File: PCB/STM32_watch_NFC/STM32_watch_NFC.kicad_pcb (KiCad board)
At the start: 4 copper layers, 37 x 37 mm, 159 parts, among them J1 Conn_01x06_Socket, J2 USB_C_Receptacle_PowerOnly_6P, Q1 2N7000, SW1 SW_DPST_x2, SW2 SW_DPST_x2, SW3 SW_DPST_x2, U1 STM32L031G6Ux, U2 MIC5365-3.3YC5, U4 MT3608, Y2 32.768kHz

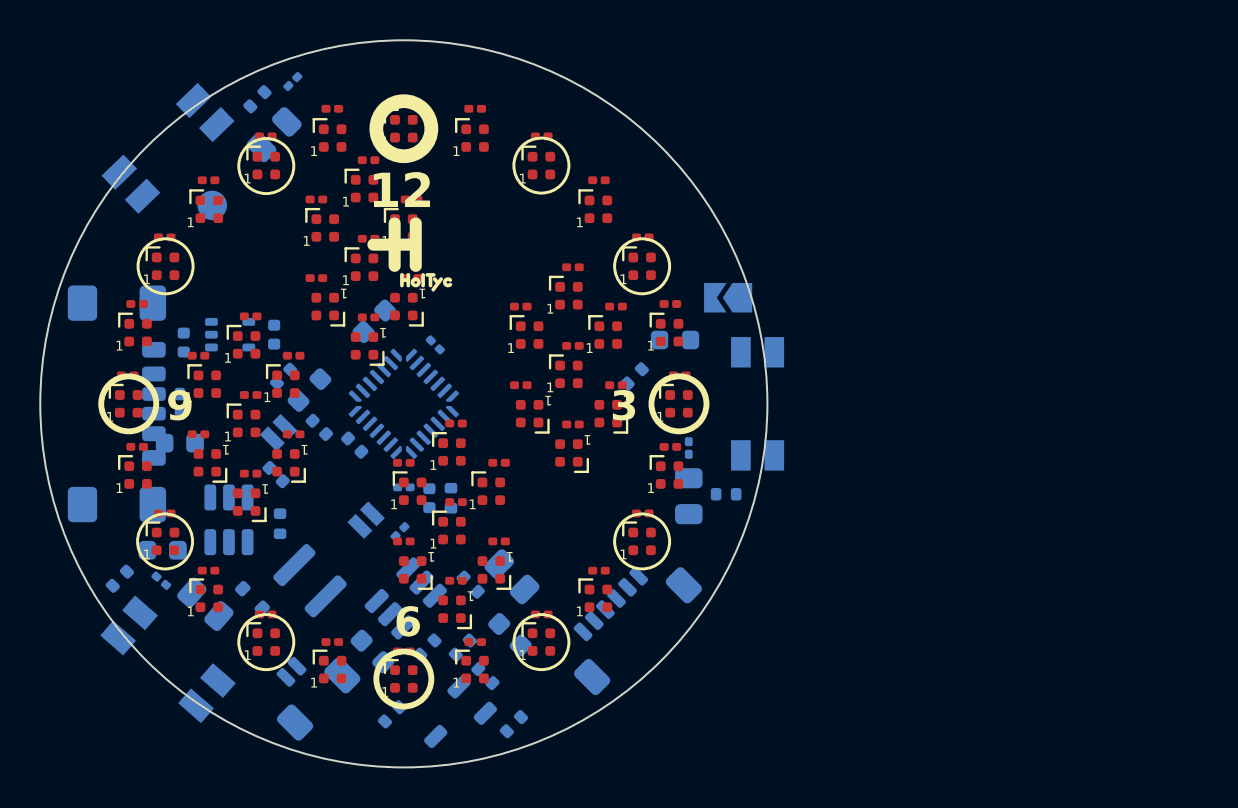
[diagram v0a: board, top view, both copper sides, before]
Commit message: Kicad - new Routing 3
TM1637 7-segment driver
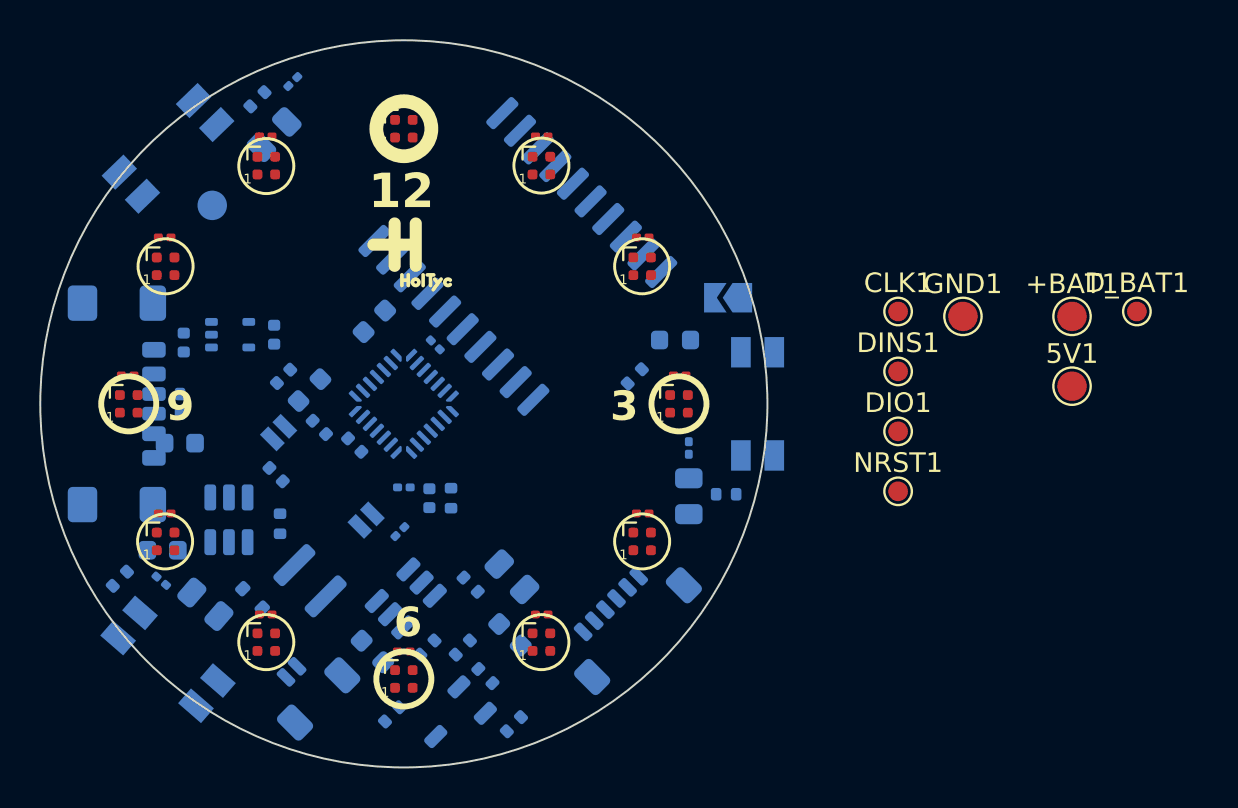
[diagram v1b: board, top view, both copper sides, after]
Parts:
- removed the C13 at (152.1, 117.1)
- removed the C15 at (158.4, 113.5)
- removed the C17 at (162.1, 107.2)
- removed the C19 at (162.1, 99.9)
- removed the C21 at (158.4, 93.6)
- removed the C23 at (152.1, 90.0)
- removed C32, C34, C36, C38, C40, C42, C43, C44, C45, C46, C47, C48, C49, C50, C51, C52, C53, C54, C55, C56, C57, C58, C59, C60, C61, C62, C63, C64, C65, C66, C67, C68, C69, C70: 100n, Capacitor_SMD:C_0201_0603Metric
- removed the D10 at (158.4, 95.1)
- removed the D12 at (152.1, 91.5)
- removed D16, D18, D20, D22, D24, D26, D27, D28, D29, D30, D31, D32, D33, D34, D35, D36, D37, D38, D39, D40, D43, D44, D45, D46, D47, D48, D49, D50, D51, D52, D53, D54: SK6805, LED_SMD:LED_SK6812_EC15_1.5x1.5mm
- removed the D2 at (152.1, 118.5)
- removed the D4 at (158.4, 114.9)
- removed the D41 at (140.5, 110.0)
- removed the D42 at (142.5, 108.0)
- removed the D6 at (162.0, 108.6)
- removed the D8 at (162.0, 101.4)
- added +BAT1: 2.7-4.2V, TestPoint:TestPoint_Pad_D1.5mm, F.Cu at (182.5, 100.5)
- added 5V1: 5V, TestPoint:TestPoint_Pad_D1.5mm, F.Cu at (182.5, 104.1)
- added CLK1: ~, TestPoint:TestPoint_Pad_D1.0mm, F.Cu at (173.7, 100.3)
- added DINS1: ~, TestPoint:TestPoint_Pad_D1.0mm, F.Cu at (173.7, 103.3)
- added DIO1: ~, TestPoint:TestPoint_Pad_D1.0mm, F.Cu at (173.7, 106.4)
- added D_BAT1: ~, TestPoint:TestPoint_Pad_D1.0mm, F.Cu at (185.8, 100.3)
- added GND1: GND, TestPoint:TestPoint_Pad_D1.5mm, F.Cu at (176.9, 100.5)
- added NRST1: ~, TestPoint:TestPoint_Pad_D1.0mm, F.Cu at (173.7, 109.5)
- added U3: TM1637, Package_SO:SOP-20_7.5x12.8mm_P1.27mm, B.Cu at (154.3, 97.5)
- renumbered C31 to C12, C22 to C13, C20 to C14, C18 to C15, C14 to C17, C12 to C18, C41 to C19, C39 to C20, C37 to C21, C35 to C22, C33 to C23, D15 to D1, D21 to D10, D19 to D11, D17 to D12, D11 to D2, D9 to D3, D7 to D4, D13 to D41, D14 to D42, D3 to D6, D1 to D7, D25 to D8, D23 to D9
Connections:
- D1 pad 1: Net-(D15-DOUT) -> Net-(D1-DOUT)
- D1 pad 3: Net-(D12-DOUT) -> Net-(D1-DIN)
- D10 pad 1: Net-(D21-DOUT) -> Net-(D10-DOUT)
- D10 pad 3: Net-(D20-DOUT) -> Net-(D10-DIN)
- D11 pad 1: Net-(D19-DOUT) -> Net-(D11-DOUT)
- D11 pad 3: Net-(D18-DOUT) -> Net-(D10-DOUT)
- D12 pad 1: Net-(D17-DOUT) -> unconnected-(D12-DOUT-Pad1)
- D12 pad 3: Net-(D16-DOUT) -> Net-(D11-DOUT)
- D2 pad 1: Net-(D11-DOUT) -> Net-(D2-DOUT)
- D2 pad 3: Net-(D10-DOUT) -> Net-(D1-DOUT)
- D3 pad 1: Net-(D10-DIN) -> Net-(D3-DOUT)
- D3 pad 3: Net-(D8-DOUT) -> Net-(D2-DOUT)
- D4 pad 1: Net-(D7-DOUT) -> Net-(D4-DOUT)
- D4 pad 3: Net-(D6-DOUT) -> Net-(D3-DOUT)
- D6 pad 1: Net-(D3-DOUT) -> Net-(D6-DOUT)
- D6 pad 3: Net-(D2-DOUT) -> Net-(D5-DOUT)
- D7 pad 1: Net-(D1-DOUT) -> Net-(D7-DOUT)
- D7 pad 3: Net-(D1-DIN) -> Net-(D6-DOUT)
- D8 pad 1: Net-(D25-DOUT) -> Net-(D8-DOUT)
- D8 pad 3: Net-(D25-DIN) -> Net-(D7-DOUT)
- D9 pad 1: Net-(D23-DOUT) -> Net-(D10-DIN)
- D9 pad 3: Net-(D22-DOUT) -> Net-(D8-DOUT)

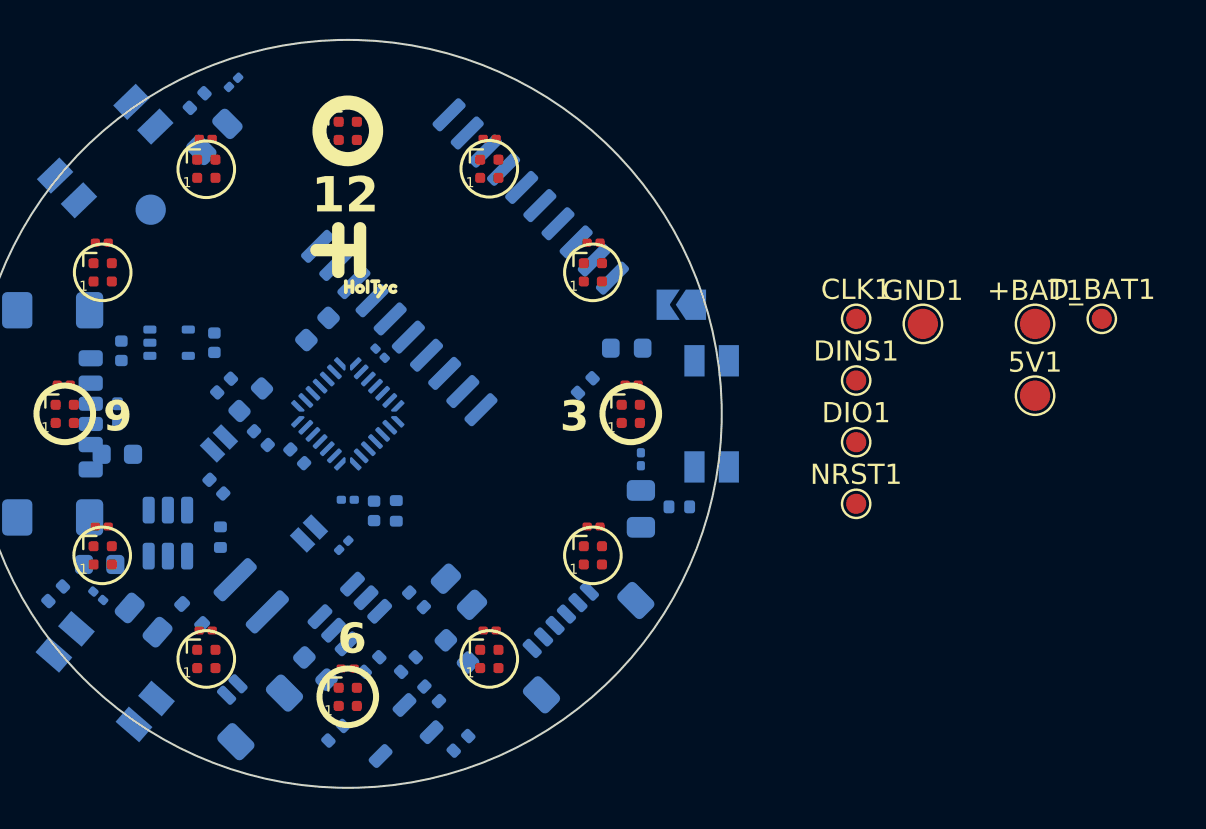
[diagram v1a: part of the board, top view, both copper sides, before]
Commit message: Kicad - new Routing 4.5
NEW 7-segment display + connection, new charger, charging status
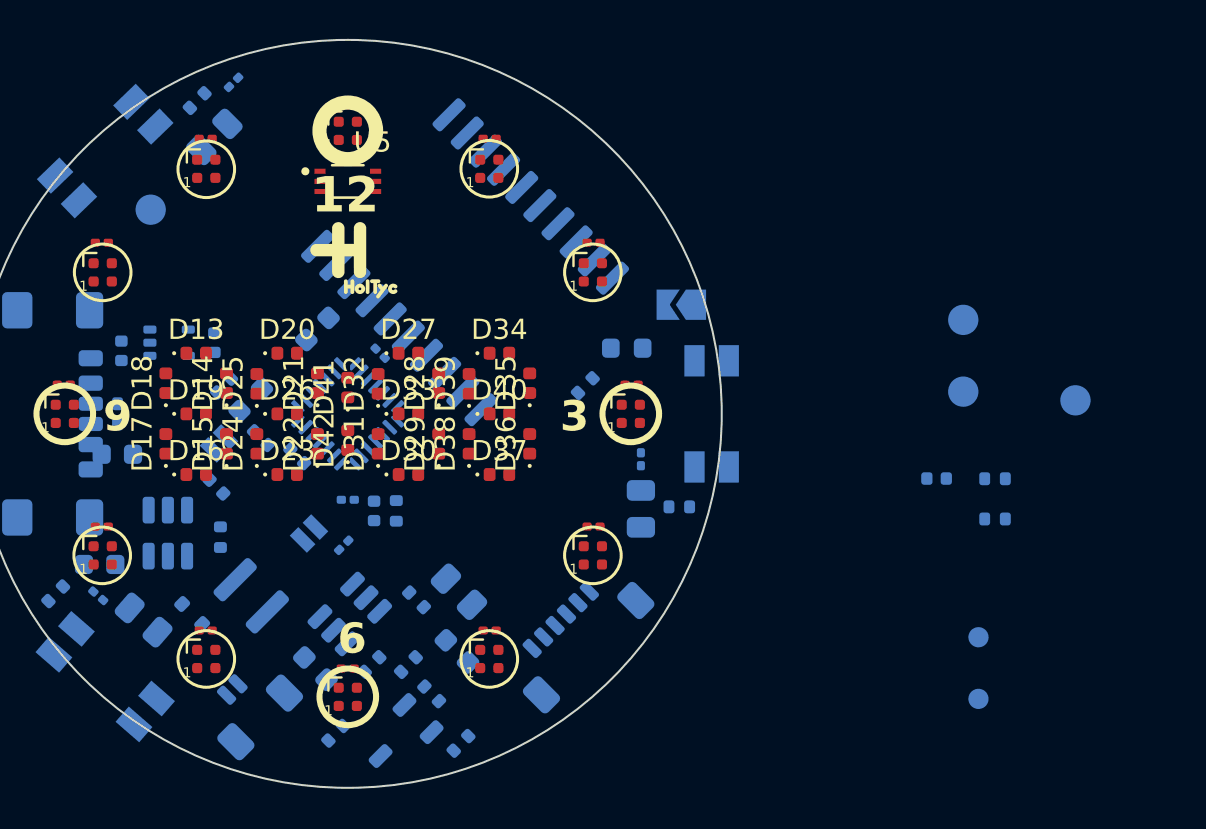
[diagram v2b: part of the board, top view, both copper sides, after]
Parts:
- removed CLK1, DINS1, DIO1, D_BAT1, NRST1: ~, TestPoint:TestPoint_Pad_D1.0mm
- added C31: 1u, Capacitor_SMD:C_0402_1005Metric, B.Cu at (177.6, 108.2)
- added D13: LED, LED_SMD:LED_0402_1005Metric, F.Cu at (141.0, 102.0)
- added D14: LED, LED_SMD:LED_0402_1005Metric, F.Cu at (142.5, 103.5)
- added D15: LED, LED_SMD:LED_0402_1005Metric, F.Cu at (142.5, 106.5)
- added D16: LED, LED_SMD:LED_0402_1005Metric, F.Cu at (141.0, 108.0)
- added D17: LED, LED_SMD:LED_0402_1005Metric, F.Cu at (139.5, 106.5)
- added D18: LED, LED_SMD:LED_0402_1005Metric, F.Cu at (139.5, 103.5)
- added D19: LED, LED_SMD:LED_0402_1005Metric, F.Cu at (141.0, 105.0)
- added D20: LED, LED_SMD:LED_0402_1005Metric, F.Cu at (145.5, 102.0)
- added D21: LED, LED_SMD:LED_0402_1005Metric, F.Cu at (147.0, 103.5)
- added D22: LED, LED_SMD:LED_0402_1005Metric, F.Cu at (147.0, 106.5)
- added D23: LED, LED_SMD:LED_0402_1005Metric, F.Cu at (145.5, 108.0)
- added D24: LED, LED_SMD:LED_0402_1005Metric, F.Cu at (144.0, 106.5)
- added D25: LED, LED_SMD:LED_0402_1005Metric, F.Cu at (144.0, 103.5)
- added D26: LED, LED_SMD:LED_0402_1005Metric, F.Cu at (145.5, 105.0)
- added D27: LED, LED_SMD:LED_0402_1005Metric, F.Cu at (151.5, 102.0)
- added D28: LED, LED_SMD:LED_0402_1005Metric, F.Cu at (153.0, 103.5)
- added D29: LED, LED_SMD:LED_0402_1005Metric, F.Cu at (153.0, 106.5)
- added D30: LED, LED_SMD:LED_0402_1005Metric, F.Cu at (151.5, 108.0)
- added D31: LED, LED_SMD:LED_0402_1005Metric, F.Cu at (150.0, 106.5)
- added D32: LED, LED_SMD:LED_0402_1005Metric, F.Cu at (150.0, 103.5)
- added D33: LED, LED_SMD:LED_0402_1005Metric, F.Cu at (151.5, 105.0)
- added D34: LED, LED_SMD:LED_0402_1005Metric, F.Cu at (156.0, 102.0)
- added D35: LED, LED_SMD:LED_0402_1005Metric, F.Cu at (157.5, 103.5)
- added D36: LED, LED_SMD:LED_0402_1005Metric, F.Cu at (157.5, 106.5)
- added D37: LED, LED_SMD:LED_0402_1005Metric, F.Cu at (156.0, 108.0)
- added D38: LED, LED_SMD:LED_0402_1005Metric, F.Cu at (154.5, 106.5)
- added D39: LED, LED_SMD:LED_0402_1005Metric, F.Cu at (154.5, 103.5)
- added D40: LED, LED_SMD:LED_0402_1005Metric, F.Cu at (156.0, 105.0)
- added D41: LED, LED_SMD:LED_0402_1005Metric, F.Cu at (148.5, 103.7)
- added D42: LED, LED_SMD:LED_0402_1005Metric, F.Cu at (148.5, 106.3)
- added DINLED1: ~, TestPoint:TestPoint_Pad_D1.0mm, B.Cu at (179.7, 116.0)
- added DINSTM2: ~, TestPoint:TestPoint_Pad_D1.0mm, B.Cu at (179.7, 119.1)
- added R20: 510, Resistor_SMD:R_0402_1005Metric, B.Cu at (180.5, 108.2)
- added R21: 510, Resistor_SMD:R_0402_1005Metric, B.Cu at (180.5, 110.2)
- added U5: BH1750FVI-TR, BH1750FVI-TR:XDCR_BH1750FVI-TR, F.Cu at (148.5, 93.5)
- +BAT1, 5V1, GND1: moved to B.Cu
- moved GND1 8.44 mm to (184.5, 104.3), turned to 180 degrees
- moved +BAT1 3.56 mm to (178.9, 100.3), turned to 180 degrees
- moved 5V1 3.56 mm to (178.9, 103.9), turned to 180 degrees
- renumbered D41 to D43, D42 to D44
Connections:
- U1 pad 25: unconnected-(U1-PB6-Pad25) -> SCL_LIGHT
- U1 pad 26: unconnected-(U1-PB7-Pad26) -> SDA_LIGHT
- U1 pad 8: unconnected-(U1-PA2-Pad8) -> LED_tecka_1
- U1 pad 9: unconnected-(U1-PA3-Pad9) -> LED_tecka_2
- U3 pad 1: unconnected-(U3-GND-Pad1) -> GND
- U3 pad 12: unconnected-(U3-GRID4-Pad12) -> GRID4
- U3 pad 13: unconnected-(U3-GRID3-Pad13) -> GRID3
- U3 pad 14: unconnected-(U3-GRID2-Pad14) -> GRID2
- U3 pad 15: unconnected-(U3-GRID1-Pad15) -> GRID1
- U3 pad 16: unconnected-(U3-VDD-Pad16) -> +5V
- U3 pad 2: unconnected-(U3-SEG1/KS1-Pad2) -> A
- U3 pad 3: unconnected-(U3-SEG2/KS2-Pad3) -> B
- U3 pad 4: unconnected-(U3-SEG3/KS3-Pad4) -> C
- U3 pad 5: unconnected-(U3-SEG4/KS4-Pad5) -> D
- U3 pad 6: unconnected-(U3-SEG5/KS5-Pad6) -> E
- U3 pad 7: unconnected-(U3-SEG6/KS6-Pad7) -> F
- U3 pad 8: unconnected-(U3-SEG7/KS7-Pad8) -> G

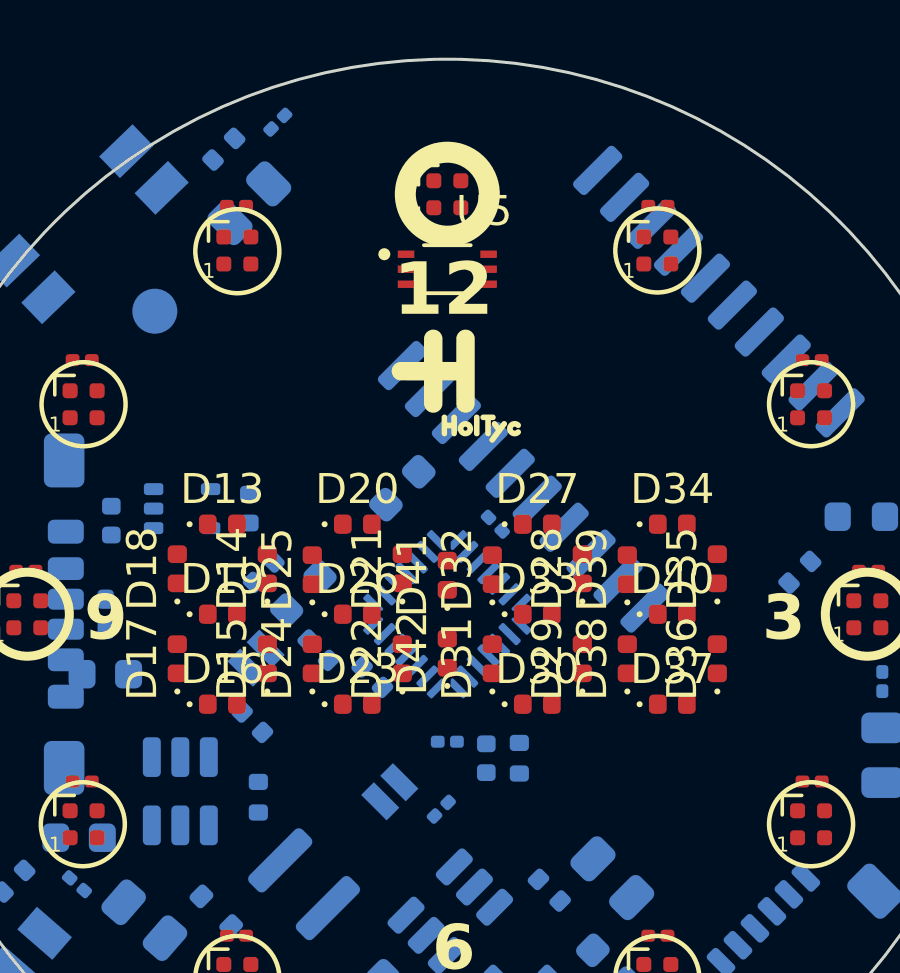
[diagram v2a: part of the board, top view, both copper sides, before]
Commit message: Kicad/STM - new Routing 5
All STM32 peripherals connected, new firmware file + new code in it :)
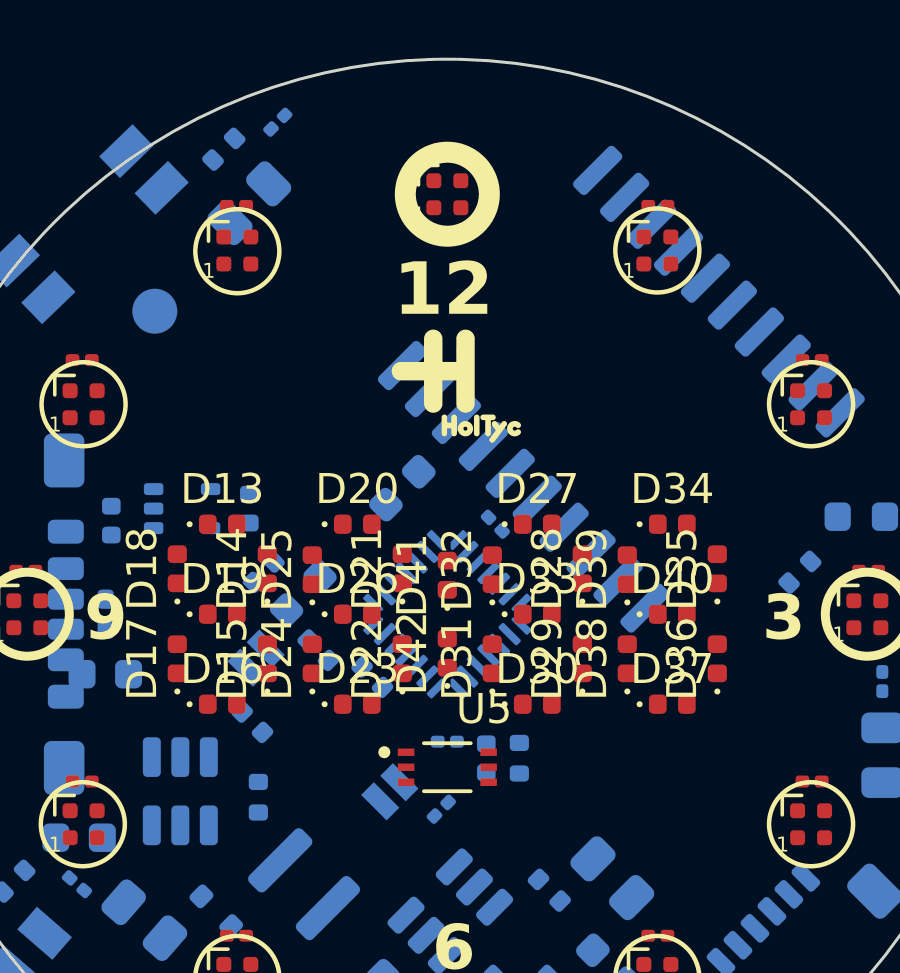
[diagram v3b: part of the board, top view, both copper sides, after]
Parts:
- moved U5 16.6 mm to (148.5, 110.1)
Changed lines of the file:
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@@
 	(footprint "BH1750FVI-TR:XDCR_BH1750FVI-TR"
 		(layer "F.Cu")
-		(at 148.5 93.5)
+		(at 148.5 110.1)
 		(property "Reference" "U5"
 			(at 1.226565 -1.937485 0)
